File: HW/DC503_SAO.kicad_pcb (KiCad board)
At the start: 2 copper layers, 63.1 x 45.1 mm, 34 parts, among them J1 GS2, J2 GS2, U1 ATTINY85-20SU, X1 Badgelife_shitty_connector

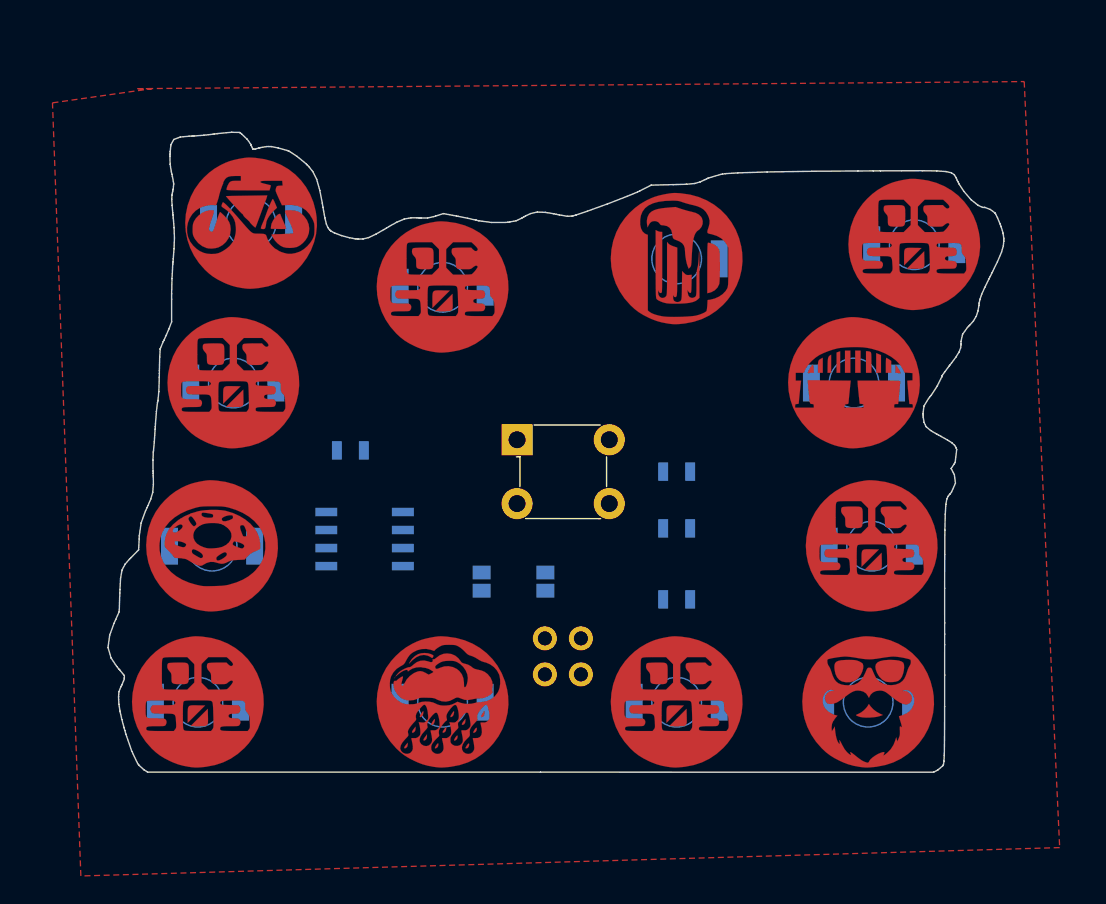
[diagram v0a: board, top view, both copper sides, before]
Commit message: Added traces to resistors
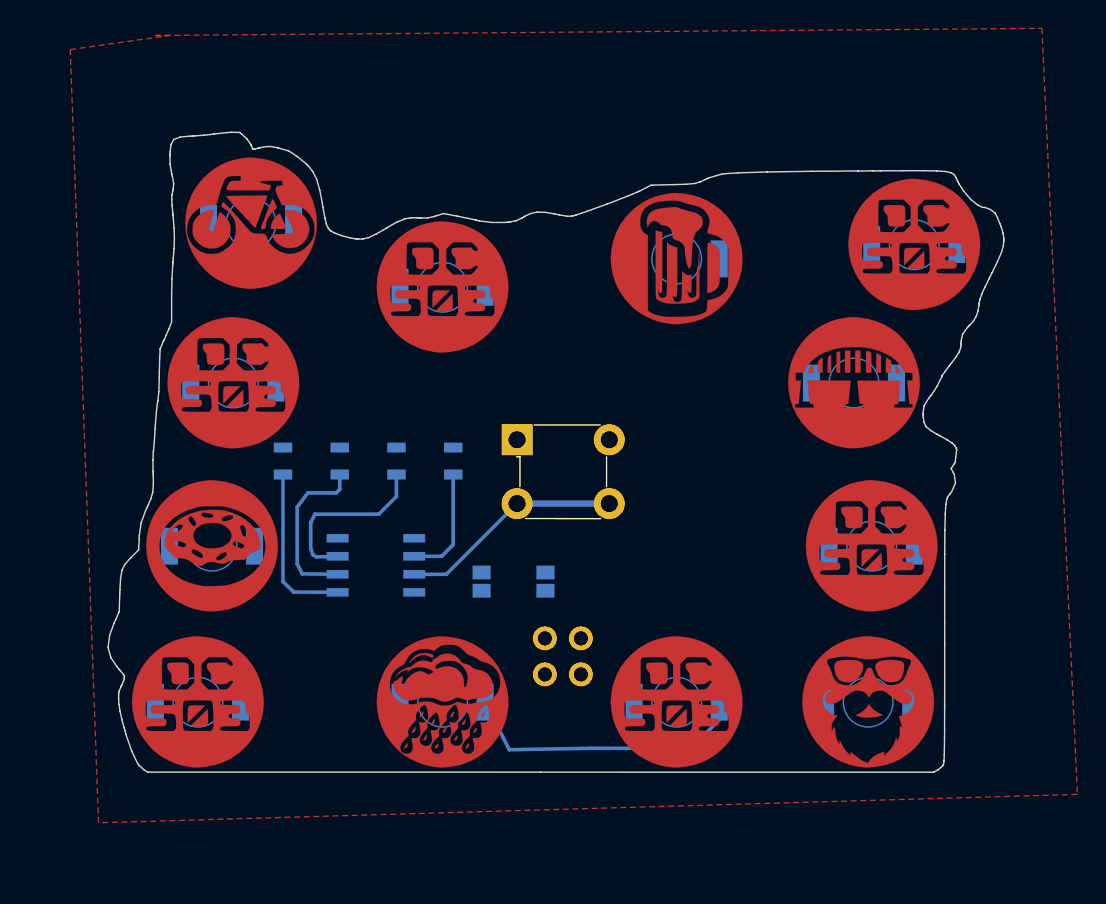
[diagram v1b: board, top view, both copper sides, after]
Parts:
- moved R1 27.8 mm to (155.2, 87.2), turned to 90 degrees
- moved R3 22.0 mm to (163.2, 87.2), turned to 90 degrees
- moved R4 16.5 mm to (167.2, 87.2), turned to 90 degrees
- moved U1 2.02 mm to (161.8, 94.6)
- moved R2 1.06 mm to (159.2, 87.2), turned to 90 degrees
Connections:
- R1 pad 1: /ROW4 -> /ROW1
- R1 pad 2: /ROW_4 -> /ROW_1
- R2 pad 1: /ROW3 -> /ROW2
- R2 pad 2: /ROW_3 -> /ROW_2
- R3 pad 1: /ROW2 -> /ROW3
- R3 pad 2: /ROW_2 -> /ROW_3
- R4 pad 1: /ROW1 -> /ROW4
- R4 pad 2: /ROW_1 -> /ROW_4
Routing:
- net /ROW_3: track 0.00 -> 20.6 mm
- net /BUTTON: track 0.00 -> 15.8 mm
- net /ROW3: track 0.00 -> 12.5 mm
- net /ROW2: track 0.00 -> 11.9 mm
- net /ROW1: track 0.00 -> 11.7 mm
- net /ROW4: track 0.00 -> 8.04 mm
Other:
- net class Default: clearance 0.2 -> 0.254; trace_width 0.25 -> 0.254; via_dia 0.6 -> 0.6858; via_drill 0.4 -> 0.3302
- net class smaller added: clearance 1.524, trace_width 1.524, via_dia 0.6858, via_drill 0.3302
- rule pad_to_mask_clearance: 0.2 -> 0.0508
- rule trace_clearance: 0.2 -> 0.254
- rule trace_min: 0.2 -> 0.1524
- rule via_min_drill: 0.3 -> 0.3302
- rule via_min_size: 0.4 -> 0.6858

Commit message: updated the LED footprint to use poly, not circle, Add traces for resistors
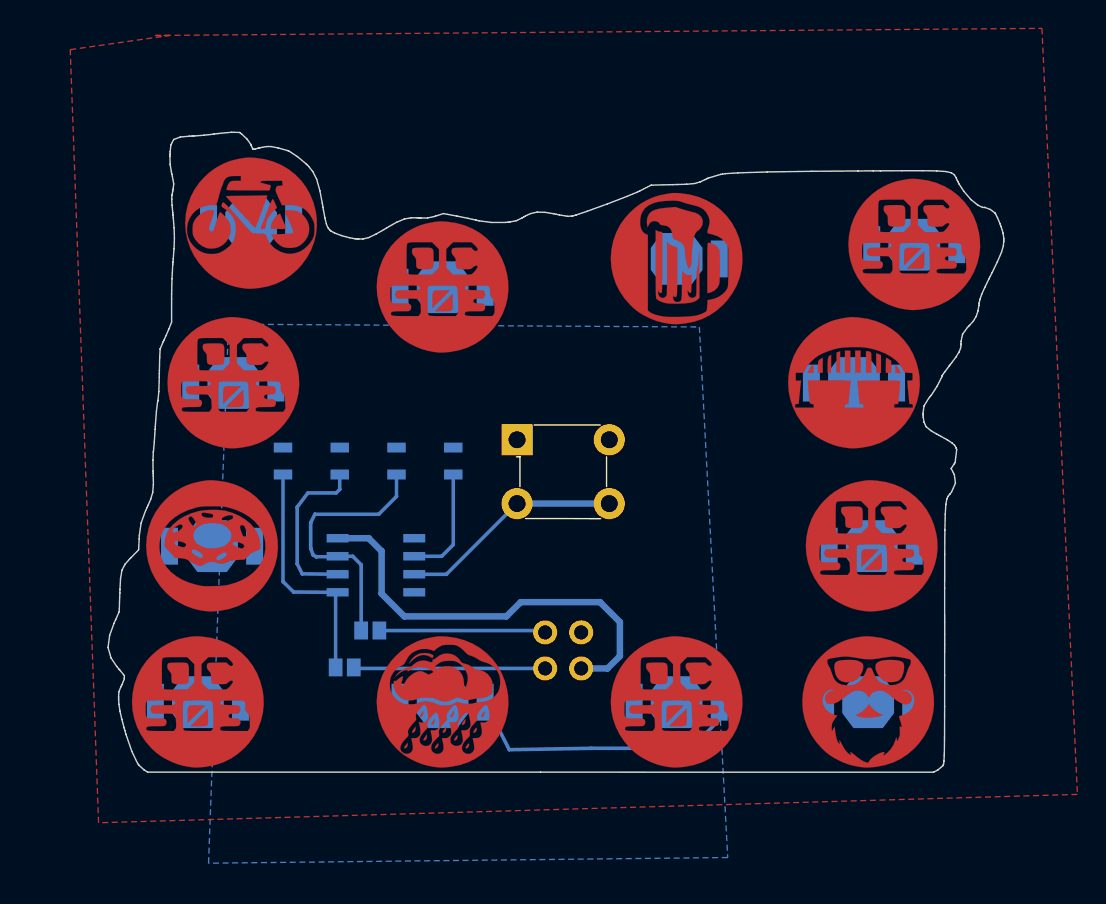
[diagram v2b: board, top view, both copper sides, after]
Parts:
- moved J1 12.8 mm to (161.4, 99.2), turned to 270 degrees
- moved J2 11.4 mm to (159.6, 101.8), turned to 270 degrees
- moved X1 0.42 mm to (175.0, 100.6)
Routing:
- net +3V3: track 0.00 -> 30.4 mm
- net Net-(J2-Pad2): track 0.00 -> 13.4 mm
- net Net-(J1-Pad2): track 0.00 -> 11.7 mm
- net /ROW3: track 12.5 -> 19.1 mm
- net /ROW1: track 11.7 -> 17.1 mm
- added copper zone on B.Cu, net GND

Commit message: Bottom gnd fill, added ROW_X traces
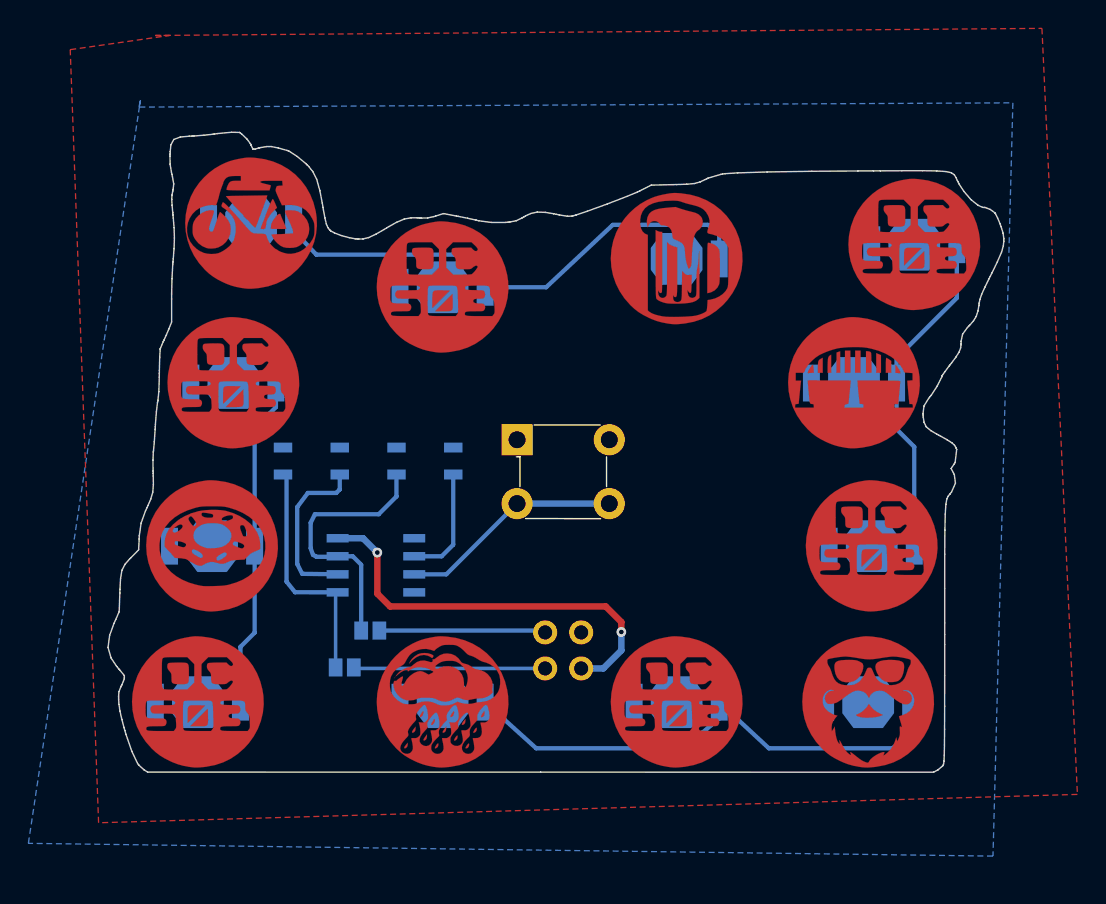
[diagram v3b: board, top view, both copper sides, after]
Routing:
- net /ROW_1: track 0.00 -> 36.6 mm
- net /ROW_4: track 0.00 -> 23.5 mm
- net /ROW_2: track 0.00 -> 23.5 mm
- net /ROW_3: track 20.6 -> 37.0 mm
- net +3V3: track 30.4 -> 29.5 mm, vias 0 -> 2

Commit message: Updated gnd plane on bottom side, connecting LEDs
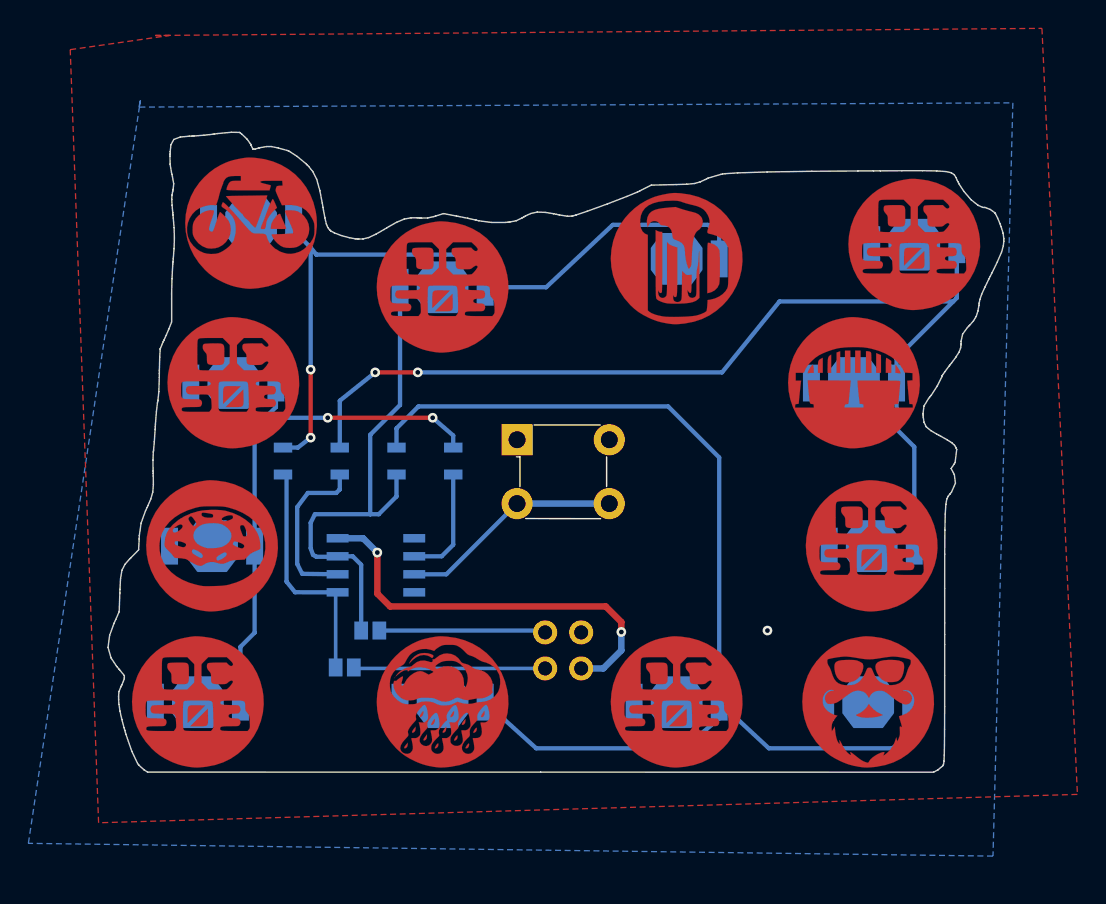
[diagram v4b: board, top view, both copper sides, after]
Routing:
- net /ROW_2: track 23.5 -> 73.2 mm, vias 0 -> 2
- net /ROW_3: track 37.0 -> 80.5 mm
- net /ROW3: track 19.1 -> 35.9 mm
- net /ROW_1: track 36.6 -> 52.0 mm, vias 0 -> 2
- net /ROW_4: track 23.5 -> 38.1 mm, vias 0 -> 2
- net GND: vias 0 -> 1

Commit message: ROW1 and ROW_1 done. Updated gnd vias.
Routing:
- net /ROW1: track 16.8 -> 118.6 mm, vias 0 -> 4
- net /ROW2: track 11.9 -> 35.8 mm
- net /ROW_3: track 80.5 -> 79.1 mm, vias 0 -> 2
- net GND: vias 1 -> 2
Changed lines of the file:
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@@
   (general
     (links 38)
-    (no_connects 12)
+    (no_connects 8)
     (area 142.865544 64.023399 206.110001 109.234705)
     (thickness 1.6002)
     (drawings 335)
-    (tracks 109)
+    (tracks 141)
     (zones 0)
     (modules 34)
@@
   (gr_line (start 205.4289 69.7478) (end 205.4621 69.7962) (layer Edge.Cuts) (width 0.1))
   (gr_line (start 204.5 75.5) (end 204.3829 75.8431) (layer Edge.Cuts) (width 0.1))
+  (segment (start 150 70.5) (end 150 76.8) (width 0.3048) (layer B.Cu) (net 1))
+  (segment (start 147.25 79.55) (end 147.25 93.25) (width 0.3048) (layer B.Cu) (net 1))
+  (segment (start 150 76.8) (end 147.25 79.55) (width 0.3048) (layer B.Cu) (net 1))
   (segment (start 159.25 88.2) (end 159.25 89.25) (width 0.3048) (layer B.Cu) (net 1))
   (segment (start 159.25 89.25) (end 159 89.5) (width 0.3048) (layer B.Cu) (net 1))
@@
   (segment (start 166.435 93.965) (end 164.5 93.965) (width 0.3048) (layer B.Cu) (net 3))
   (segment (start 167.25 93.15) (end 166.435 93.965) (width 0.3048) (layer B.Cu) (net 3))
+  (segment (start 158.96 101.8) (end 158.96 104.56) (width 0.3048) (layer B.Cu) (net 4))
+  (via (at 190.2 101.2) (size 0.6858) (drill 0.3302) (layers F.Cu B.Cu) (net 4))
+  (segment (start 190.2 104.8) (end 190.2 101.2) (width 0.3048) (layer F.Cu) (net 4))
+  (segment (start 188.2 107.4) (end 190.2 104.8) (width 0.3048) (layer F.Cu) (net 4))
+  (via (at 188.2 107.4) (size 0.6858) (drill 0.3302) (layers F.Cu B.Cu) (net 4))
+  (segment (start 161.8 107.4) (end 188.2 107.4) (width 0.3048) (layer B.Cu) (net 4))
+  (segment (start 158.96 104.56) (end 161.8 107.4) (width 0.3048) (layer B.Cu) (net 4))
+  (segment (start 190.2 101.2) (end 190.3 101.1) (width 0.3048) (layer B.Cu) (net 4))
+  (segment (start 190.3 101.1) (end 190.2 101.2) (width 0.3048) (layer B.Cu) (net 4))
+  (segment (start 190.2 101.2) (end 190.2 101) (width 0.3048) (layer B.Cu) (net 4))
+  (segment (start 193.5 104.25) (end 193.45 104.25) (width 0.3048) (layer B.Cu) (net 4))
+  (segment (start 193.45 104.25) (end 190.2 101) (width 0.3048) (layer B.Cu) (net 4))
+  (segment (start 190.2 101) (end 189.2 100) (width 0.3048) (layer B.Cu) (net 4))
+  (segment (start 189.2 100) (end 189.2 79.8) (width 0.3048) (layer B.Cu) (net 4))
+  (via (at 189.2 79.8) (size 0.6858) (drill 0.3302) (layers F.Cu B.Cu) (net 4))
+  (segment (start 189.2 79.8) (end 191.8 77.2) (width 0.3048) (layer F.Cu) (net 4))
+  (segment (start 191.8 77.2) (end 191.8 72.6) (width 0.3048) (layer F.Cu) (net 4))
+  (via (at 191.8 72.6) (size 0.6858) (drill 0.3302) (layers F.Cu B.Cu) (net 4))
+  (segment (start 191.8 72.6) (end 192.4 72) (width 0.3048) (layer B.Cu) (net 4))
+  (segment (start 192.4 72) (end 196.75 72) (width 0.3048) (layer B.Cu) (net 4))
+  (segment (start 155.5 95.75) (end 155.5 104.7) (width 0.3048) (layer B.Cu) (net 4))
+  (segment (start 146.25 106.25) (end 146.25 104.25) (width 0.3048) (layer B.Cu) (net 4))
+  (segment (start 147 107) (end 146.25 106.25) (width 0.3048) (layer B.Cu) (net 4))
+  (segment (start 153.2 107) (end 147 107) (width 0.3048) (layer B.Cu) (net 4))
+  (segment (start 155.5 104.7) (end 153.2 107) (width 0.3048) (layer B.Cu) (net 4))
   (segment (start 155.5 88.25) (end 155.5 95.75) (width 0.3048) (layer B.Cu) (net 4))
   (segment (start 156.1 96.5) (end 159.1 96.505) (width 0.3048) (layer B.Cu) (net 4))
@@
   (segment (start 173.73 101.87) (end 160.31 101.87) (width 0.254) (layer B.Cu) (net 6))
   (segment (start 160.31 101.87) (end 160.24 101.8) (width 0.254) (layer B.Cu) (net 6))
-  (via (at 189.4 99.2) (size 0.6858) (drill 0.3302) (layers F.Cu B.Cu) (net 7))
+  (via (at 155.2 76.4) (size 0.6858) (drill 0.3302) (layers F.Cu B.Cu) (net 7))
+  (via (at 191.6 87) (size 0.6858) (drill 0.3302) (layers F.Cu B.Cu) (net 7))
   (segment (start 164.5 95.235) (end 166.765 95.235) (width 0.3048) (layer B.Cu) (net 8))
   (segment (start 166.765 95.235) (end 171.75 90.25) (width 0.3048) (layer B.Cu) (net 8))
@@
   (segment (start 157.2 72.2) (end 157.2 80.8) (width 0.3048) (layer B.Cu) (net 12))
   (via (at 157.2 80.8) (size 0.6858) (drill 0.3302) (layers F.Cu B.Cu) (net 12))
-  (segment (start 156.3 86.3) (end 155.25 86.3) (width 0.3048) (layer B.Cu) (net 12) (status 800000))
+  (segment (start 156.3 86.3) (end 155.25 86.3) (width 0.3048) (layer B.Cu) (net 12))
   (via (at 157.2 85.6) (size 0.6858) (drill 0.3302) (layers F.Cu B.Cu) (net 12))
   (segment (start 156.3 86.3) (end 157.2 85.6) (width 0.3048) (layer B.Cu) (net 12))
@@
   (segment (start 198.5 80) (end 198.5 81.75) (width 0.3048) (layer B.Cu) (net 13))
   (segment (start 202.75 75.75) (end 198.5 80) (width 0.3048) (layer B.Cu) (net 13))
-  (segment (start 163.25 86.3) (end 163.25 84.95) (width 0.3048) (layer B.Cu) (net 14))
-  (segment (start 186 87) (end 186 104.25) (width 0.3048) (layer B.Cu) (net 14))
-  (segment (start 182.4 83.4) (end 186 87) (width 0.3048) (layer B.Cu) (net 14))
-  (segment (start 164.8 83.4) (end 182.4 83.4) (width 0.3048) (layer B.Cu) (net 14))
+  (segment (start 183.6 83.4) (end 184.4 84.6) (width 0.3048) (layer F.Cu) (net 14))
+  (via (at 183.6 83.4) (size 0.6858) (drill 0.3302) (layers F.Cu B.Cu) (net 14))
+  (via (at 186 87) (size 0.6858) (drill 0.3302) (layers F.Cu B.Cu) (net 14))
+  (segment (start 184.4 84.6) (end 186 87) (width 0.3048) (layer F.Cu) (net 14))
   (segment (start 163.25 84.95) (end 164.8 83.4) (width 0.3048) (layer B.Cu) (net 14))
+  (segment (start 164.8 83.4) (end 183.6 83.4) (width 0.3048) (layer B.Cu) (net 14))
+  (segment (start 186 87) (end 186 104.25) (width 0.3048) (layer B.Cu) (net 14) (status 800000))
+  (segment (start 163.25 86.3) (end 163.25 84.95) (width 0.3048) (layer B.Cu) (net 14))
   (segment (start 186 104.25) (end 186 105.4) (width 0.3048) (layer B.Cu) (net 14))
-  (segment (start 186 105.4) (end 183.5 107.5) (width 0.3048) (layer B.Cu) (net 14))
-  (segment (start 173.1 107.5) (end 169.5 104.25) (width 0.3048) (layer B.Cu) (net 14))
-  (segment (start 183.5 107.5) (end 173.1 107.5) (width 0.3048) (layer B.Cu) (net 14))
-  (segment (start 199.5 104.25) (end 199.5 106.5) (width 0.3048) (layer B.Cu) (net 14))
-  (segment (start 189.5 107.5) (end 186 104.25) (width 0.3048) (layer B.Cu) (net 14))
-  (segment (start 198.2 107.5) (end 189.5 107.5) (width 0.3048) (layer B.Cu) (net 14))
-  (segment (start 199.5 106.5) (end 198.2 107.5) (width 0.3048) (layer B.Cu) (net 14))
+  (segment (start 186 105.4) (end 183.6 106.6) (width 0.3048) (layer B.Cu) (net 14))
+  (segment (start 173.2 106.6) (end 169.5 104.25) (width 0.3048) (layer B.Cu) (net 14))
+  (segment (start 183.6 106.6) (end 173.2 106.6) (width 0.3048) (layer B.Cu) (net 14))
+  (segment (start 199.5 104.25) (end 199.445704 106.201272) (width 0.3048) (layer B.Cu) (net 14))
+  (segment (start 189.6 107) (end 186 104.25) (width 0.3048) (layer B.Cu) (net 14))
+  (segment (start 198.041357 107.100464) (end 189.6 107) (width 0.3048) (layer B.Cu) (net 14))
+  (segment (start 199.445704 106.201272) (end 198.041357 107.100464) (width 0.3048) (layer B.Cu) (net 14))
   (zone (net 7) (net_name GND) (layer F.Cu) (hatch edge 0.508)
     (connect_pads (clearance 0))
